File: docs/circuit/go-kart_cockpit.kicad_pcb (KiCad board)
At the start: 2 copper layers, 17 parts, among them J1 2x13, J2 2x13, Q1 TIP120, X1 ISP-6, X2 Bluetooth-Modul, X3 Taster links (male), X4 Taster rechts (male), X5 Display (male), X6 24V Hupe

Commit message: feat: circuit before rework with larger plate
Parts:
- removed the R5 at (110.4, 52.1)
- removed R7: 1N4004, Diode_THT:D_DO-41_SOD81_P10.16mm_Horizontal
- removed the X6 at (107.2, 31.0)
- added X3: 24V Hupe, TerminalBlock_Phoenix:TerminalBlock_Phoenix_MKDS-1,5-3-5.08_1x03_P5.08mm_Horizontal, F.Cu at (99.7, 77.5)
- R1: value 1N4148 -> 1N5817; footprint Diode_THT:D_DO-35_SOD27_P7.62mm_Horizontal -> Diode_THT:D_DO-41_SOD81_P10.16mm_Horizontal
- R2: value 10k -> 1N4936; footprint Resistor_THT:R_Axial_DIN0204_L3.6mm_D1.6mm_P7.62mm_Horizontal -> Diode_THT:D_DO-41_SOD81_P10.16mm_Horizontal
- R3: renamed from R6; value 470 10% -> 470
- X1: value ISP-6 -> AVR-ISP-10; footprint Connector_IDC:IDC-Header_2x03_P2.54mm_Horizontal -> Connector_IDC:IDC-Header_2x05_P2.54mm_Horizontal
- X2: renamed from X5; value Display (male) -> Display (2x3 male)
- X4: renamed from S1; value Start/Aus/Rückwärts -> Start/Stop/Rückwärts; footprint Connector_AMASS:AMASS_MR30PW-FB_1x03_P3.50mm_Horizontal -> TerminalBlock_Phoenix:TerminalBlock_Phoenix_MKDS-1,5-3-5.08_1x03_P5.08mm_Horizontal
- X6: renamed from X4; value Taster rechts (male) -> Taster rechts (2x5 male)
- moved R4 72.8 mm to (37.7, 53.0)
- moved X7 71.2 mm to (113.5, 35.3), turned to 0 degrees
- moved R5 70.9 mm to (42.5, 63.8), turned to 90 degrees
- moved X1 49.0 mm to (69.0, 73.0), turned to -90 degrees
- moved R1 43.9 mm to (52.0, 52.9), turned to -90 degrees
- moved X2 35.1 mm to (72.5, 32.7), turned to 90 degrees
- moved X5 34.7 mm to (64.5, 57.8), turned to -90 degrees
- moved R2 31.5 mm to (80.1, 38.5), turned to 180 degrees
- moved X4 31.0 mm to (102.0, 29.8), turned to 180 degrees
- moved X6 17.2 mm to (113.5, 58.4), turned to 0 degrees
- moved J2 7.50 mm to (28.4, 33.5)
- moved Q1 7.21 mm to (64.5, 44.0)
- moved J1 6.49 mm to (31.2, 37.0)
- moved R3 2.63 mm to (48.8, 40.0)
- renumbered R3 to R4, R4 to R5, X2 to X5, X3 to X7
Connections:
- net PC4_SW_Warnblinker renamed P_SW_BlinkerL
- net PE4_LED_Warnblinker renamed P_LED_BlinkerL
- J1 pad 15: PD2_RXD1 -> PE0_RXD0
- J1 pad 16: PD3_TXD1 -> PE1_TXD0
- J1 pad 9: Vcc (5V) -> unconnected-(J1-Pin_9-Pad9)
- J2 pad 22: unconnected-(J2-Pin_22-Pad22) -> /PE5_SW_Reverse
- J2 pad 24: PE3_LED_BlinkerR -> /PE3_SW_Start
- J2 pad 25: PE0_RXD0 -> PD2_RXD1
- J2 pad 26: PE1_TXD0 -> PD3_TXD1
- R2 pad 1: Net-(S1-4) -> +24V
- R2 pad 2: GND -> Net-(Q1-C)
- X1 pad 1: PB3_MISO -> PB2_MOSI
- X1 pad 3: PB1_SCK -> unconnected-(X1-NC-Pad3)
- X1 pad 4: PB2_MOSI -> GND
- X4 pad 1: Net-(R5-Pad1) -> /PE5_SW_Reverse
- X4 pad 2: Vcc (5V) -> GND
- X4 pad 3: Net-(S1-4) -> /PE3_SW_Start
- X6 pad 1: unconnected-(X4-Pin_1-Pad1) -> PC3_SW_BlinkerR
- X6 pad 10: unconnected-(X4-Pin_10-Pad10) -> P_LED_GearDown
- X6 pad 2: unconnected-(X4-Pin_2-Pad2) -> P_LED_BlinkerR
- X6 pad 3: unconnected-(X4-Pin_3-Pad3) -> P_SW_GearDown
- X6 pad 5: unconnected-(X4-Pin_5-Pad5) -> P_SW_GearUp
- X6 pad 7: unconnected-(X4-Pin_7-Pad7) -> GND
- X6 pad 8: unconnected-(X4-Pin_8-Pad8) -> Vcc (5V)
- X6 pad 9: unconnected-(X4-Pin_9-Pad9) -> P_LED_GearUp
- X7 pad 10: PE2_LED_BlinkerL -> P_LED_Warnblinker
- X7 pad 4: PD4_SW_LightSwitch -> P_SW_LightSwitch
- X7 pad 6: PC2_SW_BlinkerL -> P_SW_Warnblinker
- X7 pad 9: PE4_LED_LightSwitch -> P_LED_LightSwitch
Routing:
- net PB3_MISO: track 0.00 -> 96.7 mm
- net PB1_SCK: track 0.00 -> 90.9 mm
- net Vcc (5V): track 0.00 -> 68.4 mm
- net /PE5_SW_Reverse: track 0.00 -> 53.1 mm
- net /PE3_SW_Start: track 0.00 -> 38.8 mm
- net /RESET: track 0.00 -> 32.4 mm
- net Net-(R1-A): track 0.00 -> 27.2 mm
- net +24V: track 0.00 -> 25.5 mm
- net PB2_MOSI: track 0.00 -> 21.1 mm
- net Net-(Q1-B): track 0.00 -> 17.3 mm
- net PD3_TXD1: track 0.00 -> 13.9 mm
- net Net-(Q1-C): track 0.00 -> 6.76 mm
- net PB7_OC0A: track 0.00 -> 6.51 mm
- added copper zone on B.Cu, net GND

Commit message: WIP: circuit
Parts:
- added R8: 100, Resistor_THT:R_Axial_DIN0204_L3.6mm_D1.6mm_P7.62mm_Horizontal, F.Cu at (104.0, 69.8)
- added R9: 100, Resistor_THT:R_Axial_DIN0204_L3.6mm_D1.6mm_P7.62mm_Horizontal, F.Cu at (114.0, 69.8)
- moved X7 91.4 mm to (48.0, 99.2), turned to 180 degrees
- moved Q1 89.0 mm to (147.1, 77.0), turned to 90 degrees
- moved X6 67.5 mm to (48.2, 75.6), turned to 180 degrees
- moved R2 64.0 mm to (138.1, 65.7), turned to 0 degrees
- moved X2 59.9 mm to (122.9, 65.0)
- moved R1 57.1 mm to (88.9, 96.5), turned to 0 degrees
- moved R4 51.5 mm to (77.7, 85.5)
- moved R5 50.4 mm to (85.3, 90.5), turned to 180 degrees
- moved J1 50.3 mm to (71.2, 67.5)
- moved J2 50.3 mm to (68.4, 64.0)
- moved R3 50.3 mm to (88.8, 70.5)
- moved X1 50.3 mm to (109.0, 103.5)
- moved X5 49.5 mm to (105.0, 86.2)
- moved X3 42.7 mm to (138.0, 58.7), turned to 0 degrees
- moved X4 31.0 mm to (114.0, 58.4)
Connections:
- J1 pad 9: unconnected-(J1-Pin_9-Pad9) -> Vcc (5V)
- X4 pad 1: /PE5_SW_Reverse -> Net-(R9-Pad2)
- X4 pad 3: /PE3_SW_Start -> Net-(X4-4)
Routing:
- net Vcc (5V): track 68.4 -> 168.9 mm, vias 0 -> 2
- net PE0_RXD0: track 0.00 -> 54.2 mm, vias 0 -> 3
- net /PE5_SW_Reverse: track 53.1 -> 0.00 mm
- net PB3_MISO: track 96.7 -> 57.8 mm
- net /PE3_SW_Start: track 38.8 -> 0.00 mm
- net PB2_MOSI: track 21.1 -> 58.8 mm
- net PB1_SCK: track 90.9 -> 57.2 mm
- net PD2_RXD1: track 0.00 -> 27.9 mm
- net P_SW_Warnblinker: track 0.00 -> 27.0 mm
- net Net-(X5-Pin_4): track 0.00 -> 26.0 mm
- net P_SW_LightSwitch: track 0.00 -> 21.0 mm
- net P_SW_BlinkerL: track 0.00 -> 19.8 mm
- net Net-(Q1-B): track 17.3 -> 0.00 mm
- net P_LED_BlinkerL: track 0.00 -> 16.3 mm
- net P_LED_GearDown: track 0.00 -> 14.8 mm
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
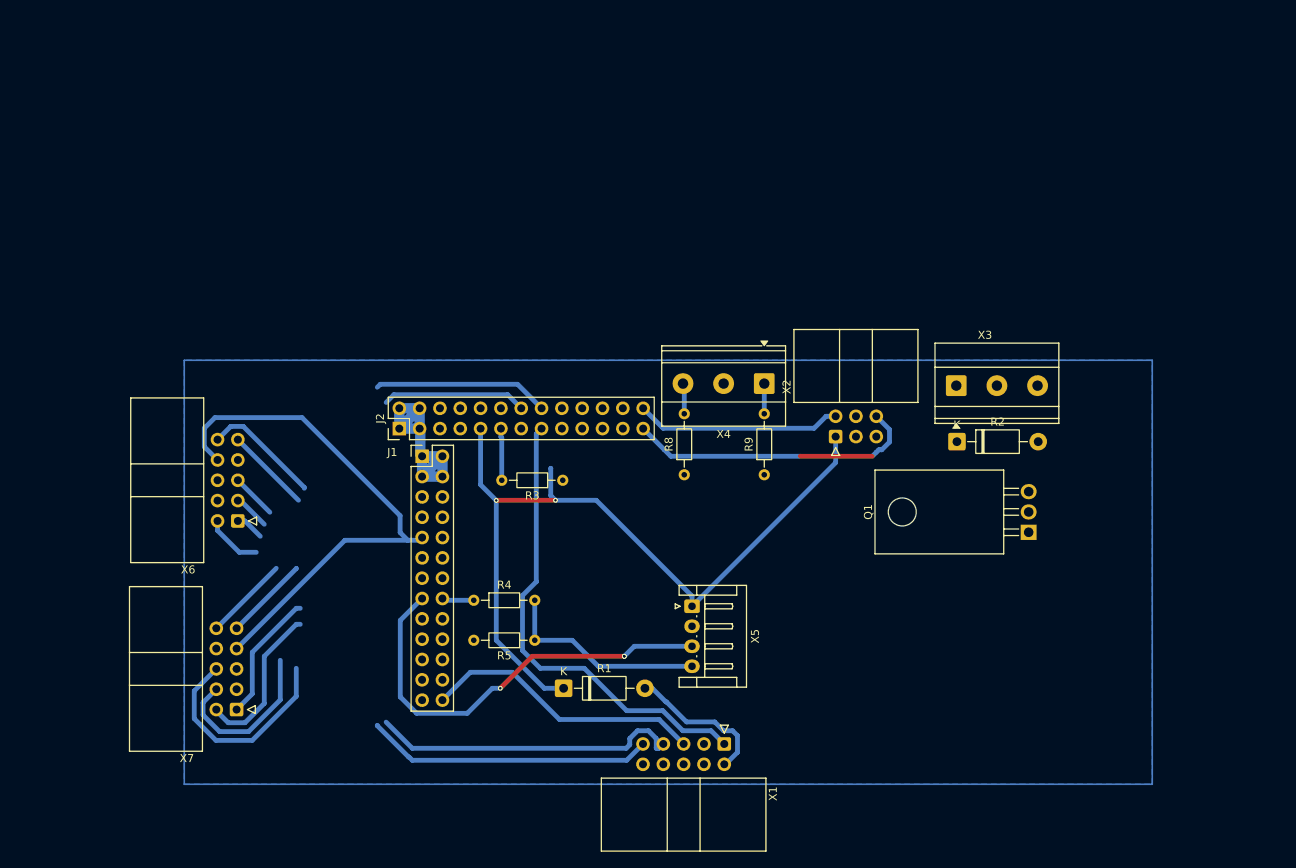
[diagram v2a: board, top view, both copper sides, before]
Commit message: feat: planned connections to MCU
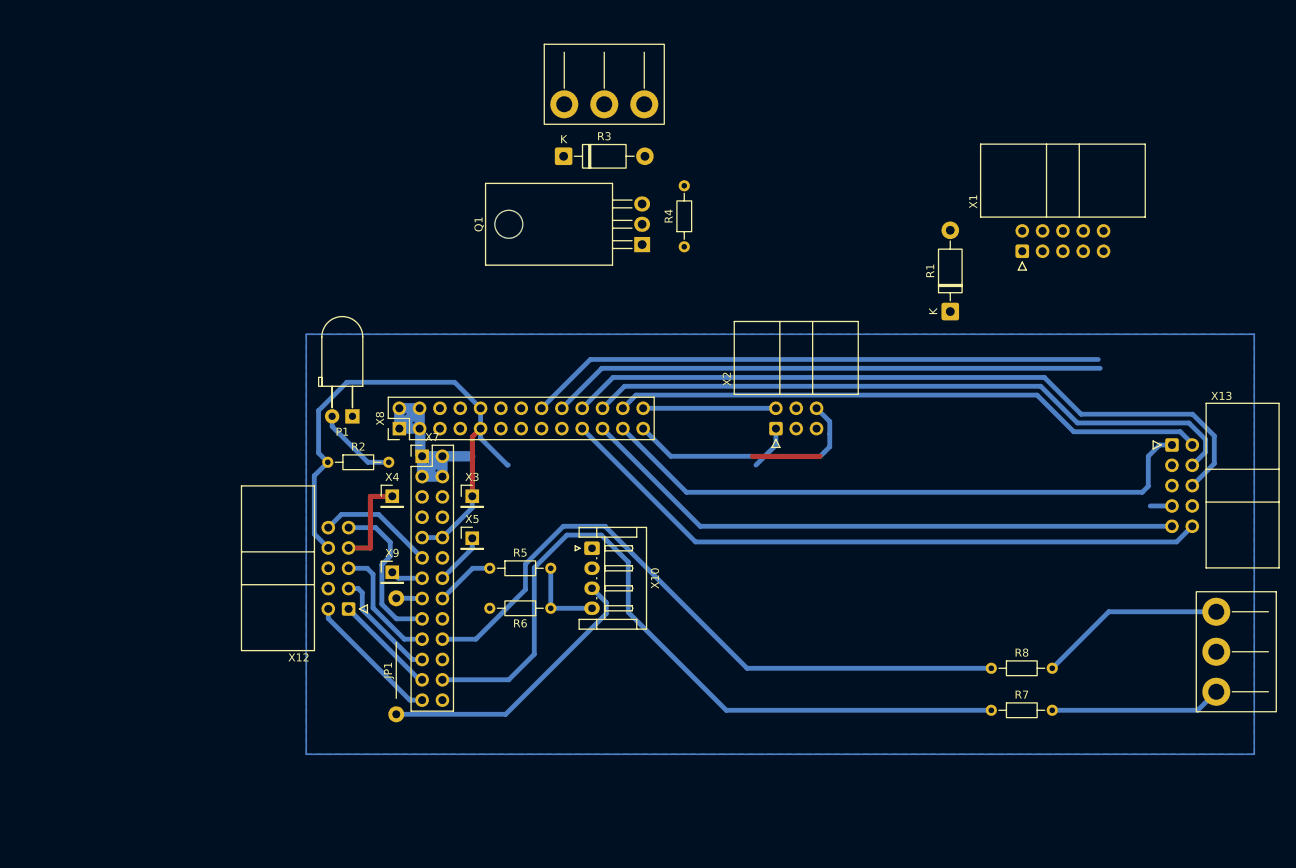
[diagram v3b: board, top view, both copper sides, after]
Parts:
- added JP1: ~, Library:Bridge, F.Cu at (68.0, 94.2)
- added P1: Power, LED_THT:LED_D5.0mm_Horizontal_O3.81mm_Z15.0mm, F.Cu at (62.5, 62.5)
- added R2: 820, Resistor_THT:R_Axial_DIN0204_L3.6mm_D1.6mm_P7.62mm_Horizontal, F.Cu at (59.4, 68.2)
- added X3: 5V, Connector_PinHeader_2.54mm:PinHeader_1x01_P2.54mm_Vertical, F.Cu at (77.5, 72.5)
- added X4: GND, Connector_PinHeader_2.54mm:PinHeader_1x01_P2.54mm_Vertical, F.Cu at (67.5, 72.5)
- added X5: SDA, Connector_PinHeader_2.54mm:PinHeader_1x01_P2.54mm_Vertical, F.Cu at (77.5, 77.8)
- added X9: SCL, Connector_PinHeader_2.54mm:PinHeader_1x01_P2.54mm_Vertical, F.Cu at (67.5, 82.0)
- Q1: footprint Package_TO_SOT_THT:TO-220F-3_Horizontal_TabDown -> Package_TO_SOT_THT:TO-220-3_Horizontal_TabDown
- X11: renamed from X4; footprint TerminalBlock_Phoenix:TerminalBlock_Phoenix_MKDS-1,5-3-5.08_1x03_P5.08mm_Horizontal -> Library:Elecbee_3pin_Green_Connector_1.5mm
- X12: renamed from X6; value Taster rechts (2x5 male) -> Taster rechts (male)
- X6: renamed from X3; footprint TerminalBlock_Phoenix:TerminalBlock_Phoenix_MKDS-1,5-3-5.08_1x03_P5.08mm_Horizontal -> Library:Elecbee_3pin_Green_Connector_1.5mm
- X7: renamed from J1; value 2x13 -> J5
- X8: renamed from J2; value 2x13 -> J3
- moved X13 121.5 mm to (165.0, 66.1), turned to 0 degrees
- moved X1 72.0 mm to (146.2, 41.9), turned to 90 degrees
- moved R1 67.5 mm to (137.2, 49.4), turned to 90 degrees
- moved X11 63.3 mm to (170.5, 86.9), turned to -90 degrees
- moved R3 60.7 mm to (88.9, 30.0)
- moved X6 60.3 mm to (89.0, 23.5)
- moved Q1 60.2 mm to (98.7, 41.0)
- moved R7 48.4 mm to (142.4, 99.2), turned to 0 degrees
- moved R8 37.3 mm to (142.4, 94.0), turned to 0 degrees
- moved R4 32.9 mm to (104.0, 41.3), turned to 90 degrees
- moved X12 17.7 mm to (62.0, 86.6)
- moved X10 14.5 mm to (92.5, 79.0)
- moved X2 7.53 mm to (115.5, 64.0)
- moved R5 4.47 mm to (79.7, 81.5)
- moved R6 4.47 mm to (87.3, 86.5)
- renumbered R2 to R3, R3 to R4, R4 to R5, R5 to R6, R8 to R7, R9 to R8, X5 to X10, X7 to X13
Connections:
- R4 pad 2: PB7_OC0A -> PB4_OC2A
- R5 pad 1: PE1_TXD0 -> PD3_TXD1
- R7 pad 1: /PE3_SW_Start -> /PC2_SW_Start
- R8 pad 1: /PE5_SW_Reverse -> /PG1_SW_Reverse
- X10 pad 3: PE0_RXD0 -> PD2_RXD1
- X12 pad 1: PC3_SW_BlinkerR -> PC0_SW_BlinkerR
- X12 pad 10: P_LED_GearDown -> PG3_LED_GearDown
- X12 pad 2: P_LED_BlinkerR -> PC3_LED_BlinkerR
- X12 pad 3: P_SW_GearDown -> PG2_SW_GearDown
- X12 pad 5: P_SW_GearUp -> PG0_SW_GearUp
- X12 pad 9: P_LED_GearUp -> PD4_LED_GearUp
- X13 pad 1: P_LED_BlinkerL -> PE2_LED_BlinkerL
- X13 pad 10: P_LED_Warnblinker -> PE6_LED_Warnblinker
- X13 pad 2: P_SW_BlinkerL -> PE3_SW_BlinkerL
- X13 pad 4: P_SW_LightSwitch -> PE5_SW_LightSwitch
- X13 pad 6: P_SW_Warnblinker -> PE7_SW_Warnblinker
- X13 pad 9: P_LED_LightSwitch -> PE4_LED_LightSwitch
- X2 pad 2: PD3_TXD1 -> PE1_TXD0
- X2 pad 6: PD2_RXD1 -> PE0_RXD0
- X7 pad 10: unconnected-(J1-Pin_10-Pad10) -> Vcc (5V)
- X7 pad 11: unconnected-(J1-Pin_11-Pad11) -> PG3_LED_GearDown
- X7 pad 13: unconnected-(J1-Pin_13-Pad13) -> /PD0_SCL
- X7 pad 14: unconnected-(J1-Pin_14-Pad14) -> /PD1_SDA
- X7 pad 15: PE0_RXD0 -> Net-(JP1-B)
- X7 pad 16: PE1_TXD0 -> PD3_TXD1
- X7 pad 17: PD4_SW_LightSwitch -> PD4_LED_GearUp
- X7 pad 19: unconnected-(J1-Pin_19-Pad19) -> PG0_SW_GearUp
- X7 pad 20: unconnected-(J1-Pin_20-Pad20) -> /PG1_SW_Reverse
- X7 pad 21: unconnected-(J1-Pin_21-Pad21) -> PG2_SW_GearDown
- X7 pad 23: unconnected-(J1-Pin_23-Pad23) -> PC0_SW_BlinkerR
- X7 pad 24: PC2_SW_BlinkerL -> /PC2_SW_Start
- X7 pad 25: PC3_SW_BlinkerR -> PC3_LED_BlinkerR
- X8 pad 10: unconnected-(J2-Pin_10-Pad10) -> Vcc (5V)
- X8 pad 11: PB7_OC0A -> unconnected-(X8-Pin_11-Pad11)
- X8 pad 13: unconnected-(J2-Pin_13-Pad13) -> PB4_OC2A
- X8 pad 14: PB1_SCK -> unconnected-(X8-Pin_14-Pad14)
- X8 pad 18: unconnected-(J2-Pin_18-Pad18) -> PB1_SCK
- X8 pad 19: unconnected-(J2-Pin_19-Pad19) -> PE6_LED_Warnblinker
- X8 pad 20: unconnected-(J2-Pin_20-Pad20) -> PE7_SW_Warnblinker
- X8 pad 22: /PE5_SW_Reverse -> PE5_SW_LightSwitch
- X8 pad 24: /PE3_SW_Start -> PE3_SW_BlinkerL
- X8 pad 25: PD2_RXD1 -> PE0_RXD0
- X8 pad 26: PD3_TXD1 -> PE1_TXD0
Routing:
- net /PC2_SW_Start: track 0.00 -> 95.2 mm
- net Vcc (5V): track 168.9 -> 77.7 mm, vias 2 -> 0
- net PE7_SW_Warnblinker: track 0.00 -> 91.0 mm
- net /PG1_SW_Reverse: track 0.00 -> 83.7 mm
- net PE5_SW_LightSwitch: track 0.00 -> 83.2 mm
- net PE6_LED_Warnblinker: track 0.00 -> 82.9 mm
- net PE2_LED_BlinkerL: track 0.00 -> 76.6 mm
- net PE4_LED_LightSwitch: track 0.00 -> 76.2 mm
- net PE3_SW_BlinkerL: track 0.00 -> 74.5 mm
- net PB2_MOSI: track 58.8 -> 0.00 mm
- net /RESET: track 35.3 -> 0.00 mm
- net PE0_RXD0: track 54.2 -> 22.2 mm, vias 3 -> 0
- net P_SW_Warnblinker: track 27.0 -> 0.00 mm
- net P_SW_LightSwitch: track 21.0 -> 0.00 mm
- net PD4_LED_GearUp: track 0.00 -> 20.2 mm
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
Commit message: feat: first sketch of PCB
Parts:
- removed JP1: ~, Library:Bridge
- added JP10: Display_Vcc, Resistor_THT:R_Axial_DIN0207_L6.3mm_D2.5mm_P7.62mm_Horizontal, F.Cu at (115.5, 81.0)
- added JP11: GND, Resistor_THT:R_Axial_DIN0207_L6.3mm_D2.5mm_P7.62mm_Horizontal, F.Cu at (64.8, 79.0)
- added JP12: Display_Vcc, Resistor_THT:R_Axial_DIN0207_L6.3mm_D2.5mm_P15.24mm_Horizontal, F.Cu at (120.0, 58.3)
- added JP2: GND, Resistor_THT:R_Axial_DIN0207_L6.3mm_D2.5mm_P15.24mm_Horizontal, F.Cu at (131.0, 57.9)
- added JP3: ISP_SCK, Resistor_THT:R_Axial_DIN0207_L6.3mm_D2.5mm_P10.16mm_Horizontal, F.Cu at (134.2, 59.8)
- added JP4: ISP_MOSI, Resistor_THT:R_Axial_DIN0207_L6.3mm_D2.5mm_P15.24mm_Horizontal, F.Cu at (144.8, 79.6)
- added JP5: TXD0, Resistor_THT:R_Axial_DIN0207_L6.3mm_D2.5mm_P10.16mm_Horizontal, F.Cu at (113.2, 67.8)
- added JP6: RXD0, Resistor_THT:R_Axial_DIN0207_L6.3mm_D2.5mm_P10.16mm_Horizontal, F.Cu at (126.2, 67.8)
- added JP8: GND, Resistor_THT:R_Axial_DIN0207_L6.3mm_D2.5mm_P10.16mm_Horizontal, F.Cu at (89.2, 81.8)
- added JP9: ~, Resistor_THT:R_Axial_DIN0207_L6.3mm_D2.5mm_P15.24mm_Horizontal, F.Cu at (67.8, 100.5)
- P1: footprint LED_THT:LED_D5.0mm_Horizontal_O3.81mm_Z15.0mm -> LED_THT:LED_D3.0mm_Horizontal_O1.27mm_Z6.0mm
- Q1: footprint Package_TO_SOT_THT:TO-220-3_Horizontal_TabDown -> Library:TO-220-3_Horizontal_TabDown_no_hole
- R4: footprint Resistor_THT:R_Axial_DIN0204_L3.6mm_D1.6mm_P7.62mm_Horizontal -> Resistor_THT:R_Axial_DIN0309_L9.0mm_D3.2mm_P25.40mm_Horizontal
- R5: footprint Resistor_THT:R_Axial_DIN0204_L3.6mm_D1.6mm_P7.62mm_Horizontal -> Resistor_THT:R_Axial_DIN0207_L6.3mm_D2.5mm_P15.24mm_Horizontal
- R6: footprint Resistor_THT:R_Axial_DIN0204_L3.6mm_D1.6mm_P7.62mm_Horizontal -> Resistor_THT:R_Axial_DIN0207_L6.3mm_D2.5mm_P10.16mm_Horizontal
- X10: footprint Connector_JST:JST_EH_S4B-EH_1x04_P2.50mm_Horizontal -> Connector_PinSocket_2.54mm:PinSocket_1x04_P2.54mm_Horizontal
- X11, X6: footprint Library:Elecbee_3pin_Green_Connector_1.5mm -> Connector_Phoenix_MC_HighVoltage:PhoenixContact_MC_1,5_3-G-5.08_1x03_P5.08mm_Horizontal
- X2: value Display (2x3 male) -> Display (male)
- X3, X4, X5, X9: footprint Connector_PinHeader_2.54mm:PinHeader_1x01_P2.54mm_Vertical -> Connector_PinSocket_2.54mm:PinSocket_1x01_P2.54mm_Vertical
- X7, X8: footprint Connector_PinHeader_2.54mm:PinHeader_2x13_P2.54mm_Vertical -> Connector_PinSocket_2.54mm:PinSocket_2x13_P2.54mm_Vertical
- moved R3 33.8 mm to (67.9, 56.5)
- moved X6 29.3 mm to (78.9, 51.0), turned to 180 degrees
- moved R1 24.5 mm to (139.0, 73.8)
- moved X10 18.1 mm to (93.6, 97.1), turned to 180 degrees
- moved Q1 17.2 mm to (85.0, 51.5), turned to -90 degrees
- moved X1 17.2 mm to (135.2, 55.0)
- moved X11 16.8 mm to (155.3, 94.0), turned to 90 degrees
- moved R6 15.9 mm to (79.5, 100.3), turned to 90 degrees
- moved X13 13.1 mm to (152.8, 61.4)
- moved R7 12.4 mm to (147.5, 87.9), turned to -90 degrees
- moved R4 10.8 mm to (108.0, 51.3), turned to -90 degrees
- moved R8 10.3 mm to (143.7, 83.8)
- moved X2 9.20 mm to (117.2, 55.0)
- moved R5 4.36 mm to (84.0, 82.1), turned to -90 degrees
- moved R2 4.10 mm to (63.5, 68.8), turned to 90 degrees
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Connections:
- R5 pad 2: Net-(X10-Pin_4) -> Net-(X10-Pin_1)
- R6 pad 1: Net-(X10-Pin_4) -> Net-(X10-Pin_1)
- R7 pad 2: Net-(X11-4) -> Net-(R7-Pad2)
- R8 pad 2: Net-(R8-Pad2) -> Net-(X11-4)
- X1 pad 1: PB2_MOSI -> Net-(JP4-B)
- X1 pad 7: PB1_SCK -> Net-(JP3-B)
- X10 pad 1: Vcc (5V) -> Net-(X10-Pin_1)
- X10 pad 2: GND -> PD2_RXD1
- X10 pad 3: PD2_RXD1 -> GND
- X10 pad 4: Net-(X10-Pin_4) -> Vcc (5V)
- X11 pad 1: Net-(R8-Pad2) -> Net-(R7-Pad2)
- X2 pad 2: PE1_TXD0 -> Net-(JP5-B)
- X2 pad 6: PE0_RXD0 -> Net-(JP6-B)
- X6 pad 2: +24V -> Net-(Q1-C)
- X6 pad 3: Net-(Q1-C) -> +24V
- X7 pad 11: PG3_LED_GearDown -> unconnected-(X7-Pin_11-Pad11)
- X7 pad 12: unconnected-(X7-Pin_12-Pad12) -> PG3_LED_GearDown
- X7 pad 13: /PD0_SCL -> /PD1_SDA
- X7 pad 14: /PD1_SDA -> /PD0_SCL
- X7 pad 15: Net-(JP1-B) -> PD3_TXD1
- X7 pad 16: PD3_TXD1 -> PD2_RXD1
- X7 pad 17: PD4_LED_GearUp -> unconnected-(X7-Pin_17-Pad17)
- X7 pad 18: unconnected-(X7-Pin_18-Pad18) -> PD4_LED_GearUp
- X7 pad 19: PG0_SW_GearUp -> /PG1_SW_Reverse
- X7 pad 20: /PG1_SW_Reverse -> PG0_SW_GearUp
- X7 pad 21: PG2_SW_GearDown -> unconnected-(X7-Pin_21-Pad21)
- X7 pad 22: unconnected-(X7-Pin_22-Pad22) -> PG2_SW_GearDown
- X7 pad 23: PC0_SW_BlinkerR -> /PC2_SW_Start
- X7 pad 24: /PC2_SW_Start -> PC0_SW_BlinkerR
- X7 pad 25: PC3_LED_BlinkerR -> /RESET
- X7 pad 26: /RESET -> PC3_LED_BlinkerR
- X8 pad 13: PB4_OC2A -> unconnected-(X8-Pin_13-Pad13)
- X8 pad 14: unconnected-(X8-Pin_14-Pad14) -> PB4_OC2A
- X8 pad 15: PB2_MOSI -> PB3_MISO
- X8 pad 16: PB3_MISO -> PB2_MOSI
- X8 pad 17: unconnected-(X8-Pin_17-Pad17) -> PB1_SCK
- X8 pad 18: PB1_SCK -> unconnected-(X8-Pin_18-Pad18)
- X8 pad 19: PE6_LED_Warnblinker -> PE7_SW_Warnblinker
- X8 pad 20: PE7_SW_Warnblinker -> PE6_LED_Warnblinker
- X8 pad 21: PE4_LED_LightSwitch -> PE5_SW_LightSwitch
- X8 pad 22: PE5_SW_LightSwitch -> PE4_LED_LightSwitch
- X8 pad 23: PE2_LED_BlinkerL -> PE3_SW_BlinkerL
- X8 pad 24: PE3_SW_BlinkerL -> PE2_LED_BlinkerL
- X8 pad 25: PE0_RXD0 -> PE1_TXD0
- X8 pad 26: PE1_TXD0 -> PE0_RXD0
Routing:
- net GND: track 12.0 -> 283.1 mm
- net /RESET: track 0.00 -> 161.1 mm
- net Vcc (5V): track 77.7 -> 228.6 mm
- net PB2_MOSI: track 0.00 -> 64.9 mm
- net PB4_OC2A: track 0.00 -> 29.5 mm
- net Net-(R8-Pad2): track 23.4 -> 0.00 mm
- net Net-(Q1-B): track 0.00 -> 23.0 mm
- net Net-(X11-4): track 21.5 -> 0.00 mm
- net PB1_SCK: track 69.4 -> 49.5 mm
- net Net-(X10-Pin_1): track 0.00 -> 15.4 mm
- net Net-(Q1-C): track 0.00 -> 15.2 mm
- net Net-(R1-A): track 0.11 -> 14.9 mm
- net Net-(JP4-B): track 0.00 -> 14.3 mm
- net +24V: track 36.6 -> 50.5 mm
- net /PC2_SW_Start: track 95.2 -> 81.5 mm
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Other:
- board outline added: 105.2 x 57.2 mm
- board text added: "JCS-BK1091_GO-KART Dean 2026 v1"

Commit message: feat(circuit): fixed DRC
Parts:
- P1: moved to B.Cu
- R2, R7, R8: footprint Resistor_THT:R_Axial_DIN0204_L3.6mm_D1.6mm_P7.62mm_Horizontal -> Resistor_THT:R_Axial_DIN0207_L6.3mm_D2.5mm_P10.16mm_Horizontal
- moved R8 8.41 mm to (149.5, 89.8), turned to 90 degrees
- moved R7 3.92 mm to (145.0, 84.9)
- moved P1 3.17 mm to (58.1, 63.5), turned to 90 degrees
- moved X11 1.44 mm to (156.0, 92.7)
- moved X13 1.21 mm to (152.7, 62.6)
- moved R2 1.00 mm to (62.5, 68.8)
- moved JP4 1.00 mm to (143.8, 79.6)
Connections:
- net Net-(Q1-C) renamed /Hupe (-)
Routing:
- net GND: track 283.1 -> 260.6 mm
- net /PG1_SW_Reverse: track 73.3 -> 86.4 mm
- net Net-(X11-4): track 0.00 -> 7.68 mm
- net /PC2_SW_Start: track 81.5 -> 77.7 mm
- net +24V: track 50.5 -> 54.1 mm
- net Net-(R7-Pad2): track 8.42 -> 11.9 mm
- net /RESET: track 161.1 -> 162.8 mm
- net Net-(JP4-B): track 14.3 -> 12.9 mm
- net PE2_LED_BlinkerL: track 67.6 -> 66.6 mm
- net PB2_MOSI: track 64.9 -> 63.9 mm
- net Net-(P1-A): track 4.78 -> 5.37 mm
- net PE6_LED_Warnblinker: track 75.7 -> 75.1 mm
- net PE4_LED_LightSwitch: track 69.9 -> 69.4 mm
